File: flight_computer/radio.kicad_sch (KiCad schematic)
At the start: 3 parts, among them J4 Conn_01x07

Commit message: Schematic connecting
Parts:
- added R15 (x2): 1M, Resistor_SMD:R_0402_1005Metric, symbol Device:R
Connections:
- net GND: now also R15.1, R15.1; no longer J4.6 (Pin_6), R1.2
- net MODE_0: now also R15.2
- net MODE_1: now also R15.2
- new net VCC: J4.6 (Pin_6), R1.2
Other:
- note added: "default pull down for normal operation"
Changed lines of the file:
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@@
 (kicad_sch (version 20230121) (generator eeschema)
   (paper "A4")
-  (junction (at 153.67 101.6) (diameter 0) (color 0 0 0 0)
-  )
   (junction (at 147.32 99.06) (diameter 0) (color 0 0 0 0)
   )
+  (junction (at 140.97 88.9) (diameter 0) (color 0 0 0 0)
+  )
+  (junction (at 151.13 118.11) (diameter 0) (color 0 0 0 0)
+  )
+  (junction (at 140.97 76.2) (diameter 0) (color 0 0 0 0)
+  )
   (junction (at 124.46 96.52) (diameter 0) (color 0 0 0 0)
   )
-  (junction (at 153.67 99.06) (diameter 0) (color 0 0 0 0)
-  )
-  (wire (pts (xy 119.38 86.36) (xy 153.67 86.36))
-    (stroke (width 0) (type default))
-  )
-  (wire (pts (xy 153.67 101.6) (xy 153.67 99.06))
+  (junction (at 133.35 86.36) (diameter 0) (color 0 0 0 0)
+  )
+  (wire (pts (xy 119.38 86.36) (xy 133.35 86.36))
+    (stroke (width 0) (type default))
+  )
+  (wire (pts (xy 133.35 78.74) (xy 133.35 76.2))
+    (stroke (width 0) (type default))
+  )
+  (wire (pts (xy 176.53 118.11) (xy 151.13 118.11))
     (stroke (width 0) (type default))
   )
@@
     (stroke (width 0) (type default))
   )
-  (wire (pts (xy 151.13 118.11) (xy 151.13 101.6))
-    (stroke (width 0) (type default))
-  )
-  (wire (pts (xy 119.38 88.9) (xy 153.67 88.9))
+  (wire (pts (xy 176.53 76.2) (xy 176.53 118.11))
+    (stroke (width 0) (type default))
+  )
+  (wire (pts (xy 140.97 88.9) (xy 153.67 88.9))
+    (stroke (width 0) (type default))
+  )
+  (wire (pts (xy 151.13 101.6) (xy 151.13 118.11))
+    (stroke (width 0) (type default))
+  )
+  (wire (pts (xy 119.38 88.9) (xy 140.97 88.9))
     (stroke (width 0) (type default))
   )
@@
     (stroke (width 0) (type default))
   )
+  (wire (pts (xy 140.97 81.28) (xy 140.97 76.2))
+    (stroke (width 0) (type default))
+  )
+  (wire (pts (xy 140.97 76.2) (xy 176.53 76.2))
+    (stroke (width 0) (type default))
+  )
+  (wire (pts (xy 133.35 76.2) (xy 140.97 76.2))
+    (stroke (width 0) (type default))
+  )
   (wire (pts (xy 151.13 101.6) (xy 153.67 101.6))
     (stroke (width 0) (type default))
@@
   )
   (wire (pts (xy 119.38 96.52) (xy 124.46 96.52))
+    (stroke (width 0) (type default))
+  )
+  (wire (pts (xy 133.35 86.36) (xy 153.67 86.36))
     (stroke (width 0) (type default))
   )
@@
     (effects (font (size 1.27 1.27)) (justify left bottom))
   )
+  (text "default pull down for normal operation" (at 130.81 74.93 0)
+    (effects (font (size 1.27 1.27)) (justify left bottom))
+  )
   (text "AUX low when busy" (at 91.44 97.79 0)
     (effects (font (size 1.27 1.27)) (justify left bottom))
@@
   (hierarchical_label "TXD" (shape output) (at 119.38 93.98 180) (fields_autoplaced)
     (effects (font (size 1.27 1.27)) (justify right))
+  )
+  (symbol (lib_id "Device:R") (at 133.35 82.55 0) (unit 1)
+    (in_bom yes) (on_board yes) (dnp no) (fields_autoplaced)
+    (property "Reference" "R15" (at 135.89 81.28 0)
+      (effects (font (size 1.27 1.27)) (justify left))
+    )
+    (property "Value" "1M" (at 135.89 83.82 0)
+      (effects (font (size 1.27 1.27)) (justify left))
+    )
+    (property "Footprint" "Resistor_SMD:R_0402_1005Metric" (at 131.572 82.55 90)
+      (effects (font (size 1.27 1.27)) hide)
+    )
+    (property "Datasheet" "https://wmsc.lcsc.com/wmsc/upload/file/pdf/v2/lcsc/2206010030_UNI-ROYAL-Uniroyal-Elec-0402WGF1004TCE_C26083.pdf" (at 133.35 82.55 0)
+      (effects (font (size 1.27 1.27)) hide)
+    )
+    (property "Manufacturer PN" "0402WGF1004TCE" (at 133.35 82.55 0)
+      (effects (font (size 1.27 1.27)) hide)
+    )
+    (property "Supplier PN" "C26083" (at 133.35 82.55 0)
+      (effects (font (size 1.27 1.27)) hide)
+    )
+    (property "Supplier" "JLC" (at 133.35 82.55 0)
+      (effects (font (size 1.27 1.27)) hide)
+    )
+    (pin "1")
+    (pin "2")
+    (instances
+      (project "flight_computer"
+        (path "/89a81c02-14e9-456f-a334-ff69a24bd093/ebc948db-a9d3-410a-bdbf-1c31db890e56"
+          (reference "R15") (unit 1)
+        )
+        (path "/89a81c02-14e9-456f-a334-ff69a24bd093/0b835f18-e97c-4530-9363-7eee1af6da75"
+          (reference "R22") (unit 1)
+        )
+      )
+    )
   )
   (symbol (lib_id "Device:R") (at 138.43 99.06 90) (mirror x) (unit 1)
@@
         )
       )
+    )
+  )
+  (symbol (lib_id "Device:R") (at 140.97 85.09 0) (unit 1)
+    (in_bom yes) (on_board yes) (dnp no) (fields_autoplaced)
+    (property "Reference" "R15" (at 143.51 83.82 0)
+      (effects (font (size 1.27 1.27)) (justify left))
+    )
+    (property "Value" "1M" (at 143.51 86.36 0)
+      (effects (font (size 1.27 1.27)) (justify left))
+    )
+    (property "Footprint" "Resistor_SMD:R_0402_1005Metric" (at 139.192 85.09 90)
+      (effects (font (size 1.27 1.27)) hide)
+    )
+    (property "Datasheet" "https://wmsc.lcsc.com/wmsc/upload/file/pdf/v2/lcsc/2206010030_UNI-ROYAL-Uniroyal-Elec-0402WGF1004TCE_C26083.pdf" (at 140.97 85.09 0)
+      (effects (font (size 1.27 1.27)) hide)
+    )
+    (property "Manufacturer PN" "0402WGF1004TCE" (at 140.97 85.09 0)
+      (effects (font (size 1.27 1.27)) hide)
+    )
+    (property "Supplier PN" "C26083" (at 140.97 85.09 0)
+      (effects (font (size 1.27 1.27)) hide)
+    )
+    (property "Supplier" "JLC" (at 140.97 85.09 0)
+      (effects (font (size 1.27 1.27)) hide)
+    )
+    (pin "1")
+    (pin "2")
+    (instances
+      (project "flight_computer"
+        (path "/89a81c02-14e9-456f-a334-ff69a24bd093/ebc948db-a9d3-410a-bdbf-1c31db890e56"
+          (reference "R15") (unit 1)
+        )
+        (path "/89a81c02-14e9-456f-a334-ff69a24bd093/0b835f18-e97c-4530-9363-7eee1af6da75"
+          (reference "R23") (unit 1)
+        )
+      )

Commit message: Part way through review
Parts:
- J4: footprint (none) -> Connector_PinHeader_2.54mm:PinHeader_1x07_P2.54mm_Vertical; now left out of the parts list
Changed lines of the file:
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@@
         )
         (path "/89a81c02-14e9-456f-a334-ff69a24bd093/0b835f18-e97c-4530-9363-7eee1af6da75"
-          (reference "R22") (unit 1)
+          (reference "R21") (unit 1)
         )
       )
@@
         )
         (path "/89a81c02-14e9-456f-a334-ff69a24bd093/0b835f18-e97c-4530-9363-7eee1af6da75"
-          (reference "R18") (unit 1)
+          (reference "R22") (unit 1)
         )
       )
@@
   )
   (symbol (lib_id "Connector_Generic:Conn_01x07") (at 158.75 93.98 0) (unit 1)
-    (in_bom yes) (on_board yes) (dnp no) (fields_autoplaced)
+    (in_bom no) (on_board yes) (dnp no) (fields_autoplaced)
     (property "Reference" "J4" (at 161.29 92.71 0)
       (effects (font (size 1.27 1.27)) (justify left))
@@
       (effects (font (size 1.27 1.27)) (justify left))
     )
-    (property "Footprint" "" (at 158.75 93.98 0)
+    (property "Footprint" "Connector_PinHeader_2.54mm:PinHeader_1x07_P2.54mm_Vertical" (at 158.75 93.98 0)
       (effects (font (size 1.27 1.27)) hide)
     )
@@
       (effects (font (size 1.27 1.27)) hide)
     )
+    (property "Manufacturer PN" "~" (at 158.75 93.98 0)
+      (effects (font (size 1.27 1.27)) hide)
+    )
+    (property "Supplier PN" "~" (at 158.75 93.98 0)
+      (effects (font (size 1.27 1.27)) hide)
+    )
+    (property "Supplier" "~" (at 158.75 93.98 0)
+      (effects (font (size 1.27 1.27)) hide)
+    )

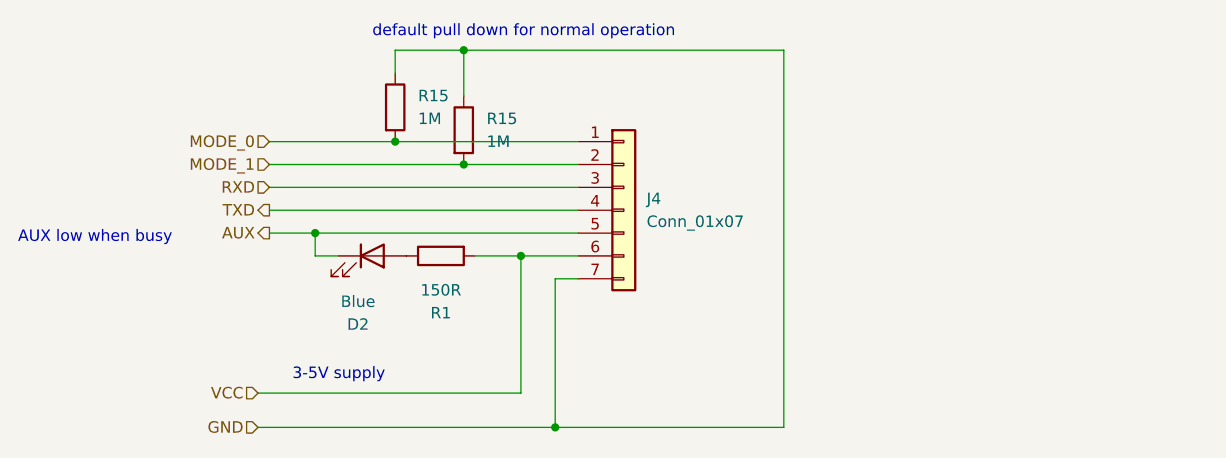
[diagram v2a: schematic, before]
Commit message: finsihed grouping the layout
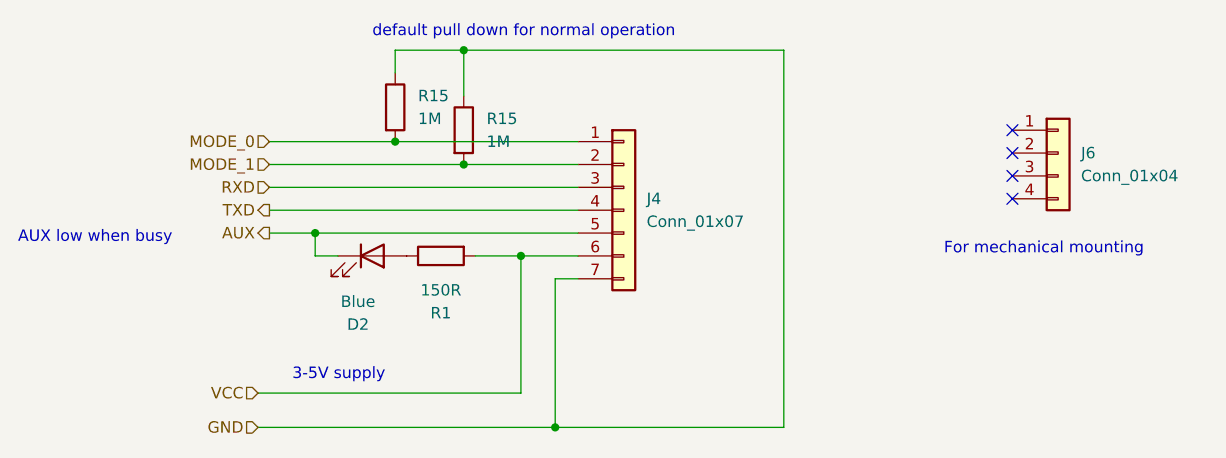
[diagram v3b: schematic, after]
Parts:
- added J6: Conn_01x04, Connector_PinHeader_2.54mm:PinHeader_1x04_P2.54mm_Vertical, symbol Connector_Generic:Conn_01x04
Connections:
- no-connect marks 0 -> 4
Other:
- note added: "For mechanical mounting"
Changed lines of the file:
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@@
   (junction (at 133.35 86.36) (diameter 0) (color 0 0 0 0)
   )
+  (no_connect (at 201.93 87.63))
+  (no_connect (at 201.93 85.09))
+  (no_connect (at 201.93 90.17))
+  (no_connect (at 201.93 92.71))
   (wire (pts (xy 119.38 86.36) (xy 133.35 86.36))
     (stroke (width 0) (type default))
@@
     (effects (font (size 1.27 1.27)) (justify left bottom))
   )
+  (text "For mechanical mounting" (at 194.31 99.06 0)
+    (effects (font (size 1.27 1.27)) (justify left bottom))
+  )
   (hierarchical_label "VCC" (shape input) (at 118.11 114.3 180) (fields_autoplaced)
     (effects (font (size 1.27 1.27)) (justify right))
@@
     (effects (font (size 1.27 1.27)) (justify right))
   )
+  (symbol (lib_id "Connector_Generic:Conn_01x04") (at 207.01 87.63 0) (unit 1)
+    (in_bom no) (on_board yes) (dnp no) (fields_autoplaced)
+    (property "Reference" "J6" (at 209.55 87.63 0)
+      (effects (font (size 1.27 1.27)) (justify left))
+    )
+    (property "Value" "Conn_01x04" (at 209.55 90.17 0)
+      (effects (font (size 1.27 1.27)) (justify left))
+    )
+    (property "Footprint" "Connector_PinHeader_2.54mm:PinHeader_1x04_P2.54mm_Vertical" (at 207.01 87.63 0)
+      (effects (font (size 1.27 1.27)) hide)
+    )
+    (property "Datasheet" "~" (at 207.01 87.63 0)
+      (effects (font (size 1.27 1.27)) hide)
+    )
+    (property "Manufacturer PN" "~" (at 207.01 87.63 0)
+      (effects (font (size 1.27 1.27)) hide)
+    )
+    (property "Supplier PN" "~" (at 207.01 87.63 0)
+      (effects (font (size 1.27 1.27)) hide)
+    )
+    (property "Supplier" "~" (at 207.01 87.63 0)
+      (effects (font (size 1.27 1.27)) hide)
+    )
+    (pin "1")
+    (pin "2")
+    (pin "3")
+    (pin "4")
+    (instances
+      (project "flight_computer"
+        (path "/89a81c02-14e9-456f-a334-ff69a24bd093/0b835f18-e97c-4530-9363-7eee1af6da75"
+          (reference "J6") (unit 1)
+        )
+      )
+    )
+  )
   (symbol (lib_id "Device:R") (at 133.35 82.55 0) (unit 1)

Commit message: Layout first effort done
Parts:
- added C1: 100nF, Capacitor_SMD:C_0402_1005Metric, symbol Device:C
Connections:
- net GND: now also C1.2
- net VCC: now also C1.1
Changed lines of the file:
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@@
 (kicad_sch (version 20230121) (generator eeschema)
   (paper "A4")
-  (junction (at 147.32 99.06) (diameter 0) (color 0 0 0 0)
-  )
   (junction (at 140.97 88.9) (diameter 0) (color 0 0 0 0)
   )
   (junction (at 151.13 118.11) (diameter 0) (color 0 0 0 0)
   )
+  (junction (at 148.59 99.06) (diameter 0) (color 0 0 0 0)
+  )
   (junction (at 140.97 76.2) (diameter 0) (color 0 0 0 0)
+  )
+  (junction (at 138.43 118.11) (diameter 0) (color 0 0 0 0)
+  )
+  (junction (at 138.43 110.49) (diameter 0) (color 0 0 0 0)
   )
   (junction (at 124.46 96.52) (diameter 0) (color 0 0 0 0)
@@
     (stroke (width 0) (type default))
   )
-  (wire (pts (xy 147.32 114.3) (xy 147.32 99.06))
+  (wire (pts (xy 138.43 118.11) (xy 151.13 118.11))
+    (stroke (width 0) (type default))
+  )
+  (wire (pts (xy 148.59 110.49) (xy 148.59 99.06))
+    (stroke (width 0) (type default))
+  )
+  (wire (pts (xy 138.43 110.49) (xy 148.59 110.49))
+    (stroke (width 0) (type default))
+  )
+  (wire (pts (xy 148.59 99.06) (xy 153.67 99.06))
     (stroke (width 0) (type default))
   )
@@
     (stroke (width 0) (type default))
   )
-  (wire (pts (xy 142.24 99.06) (xy 147.32 99.06))
-    (stroke (width 0) (type default))
-  )
   (wire (pts (xy 140.97 81.28) (xy 140.97 76.2))
     (stroke (width 0) (type default))
@@
     (stroke (width 0) (type default))
   )
-  (wire (pts (xy 118.11 118.11) (xy 151.13 118.11))
+  (wire (pts (xy 118.11 118.11) (xy 138.43 118.11))
     (stroke (width 0) (type default))
   )
@@
     (stroke (width 0) (type default))
   )
-  (wire (pts (xy 118.11 114.3) (xy 147.32 114.3))
+  (wire (pts (xy 142.24 99.06) (xy 148.59 99.06))
+    (stroke (width 0) (type default))
+  )
+  (wire (pts (xy 118.11 110.49) (xy 138.43 110.49))
     (stroke (width 0) (type default))
   )
@@
     (stroke (width 0) (type default))
   )
-  (wire (pts (xy 147.32 99.06) (xy 153.67 99.06))
-    (stroke (width 0) (type default))
-  )
-  (text "3-5V supply" (at 121.92 113.03 0)
+  (text "3-5V supply" (at 123.19 109.22 0)
     (effects (font (size 1.27 1.27)) (justify left bottom))
   )
@@
     (effects (font (size 1.27 1.27)) (justify left bottom))
   )
-  (hierarchical_label "VCC" (shape input) (at 118.11 114.3 180) (fields_autoplaced)
+  (hierarchical_label "VCC" (shape input) (at 118.11 110.49 180) (fields_autoplaced)
     (effects (font (size 1.27 1.27)) (justify right))
   )
@@
         )
       )
+    )
+  )
+  (symbol (lib_id "Device:C") (at 138.43 114.3 0) (unit 1)
+    (in_bom yes) (on_board yes) (dnp no)
+    (property "Reference" "C1" (at 142.24 113.03 0)
+      (effects (font (size 1.27 1.27)) (justify left))
+    )
+    (property "Value" "100nF" (at 142.24 115.57 0)
+      (effects (font (size 1.27 1.27)) (justify left))
+    )
+    (property "Footprint" "Capacitor_SMD:C_0402_1005Metric" (at 139.3952 118.11 0)
+      (effects (font (size 1.27 1.27)) hide)
+    )
+    (property "Datasheet" "https://wmsc.lcsc.com/wmsc/upload/file/pdf/v2/lcsc/2304140030_Samsung-Electro-Mechanics-CL05B104KO5NNNC_C1525.pdf" (at 138.43 114.3 0)
+      (effects (font (size 1.27 1.27)) hide)
+    )
+    (property "Manufacturer PN" "CL05B104KO5NNNC" (at 138.43 114.3 0)
+      (effects (font (size 1.27 1.27)) hide)
+    )
+    (property "Supplier PN" "C1525" (at 138.43 114.3 0)
+      (effects (font (size 1.27 1.27)) hide)
+    )
+    (property "Supplier" "JLC" (at 138.43 114.3 0)
+      (effects (font (size 1.27 1.27)) hide)
+    )
+    (property "Voltage" "16V" (at 133.35 114.3 0)
+      (effects (font (size 1.27 1.27)))
+    )
+    (pin "1")
+    (pin "2")
+    (instances
+      (project "flight_computer"
+        (path "/89a81c02-14e9-456f-a334-ff69a24bd093/ebc948db-a9d3-410a-bdbf-1c31db890e56"
+          (reference "C1") (unit 1)
+        )
+        (path "/89a81c02-14e9-456f-a334-ff69a24bd093/60625ff5-21c7-44a3-8ce9-cc38254a738b"
+          (reference "C4") (unit 1)
+        )
+        (path "/89a81c02-14e9-456f-a334-ff69a24bd093/0b835f18-e97c-4530-9363-7eee1af6da75"
+          (reference "C38") (unit 1)
+        )
+      )

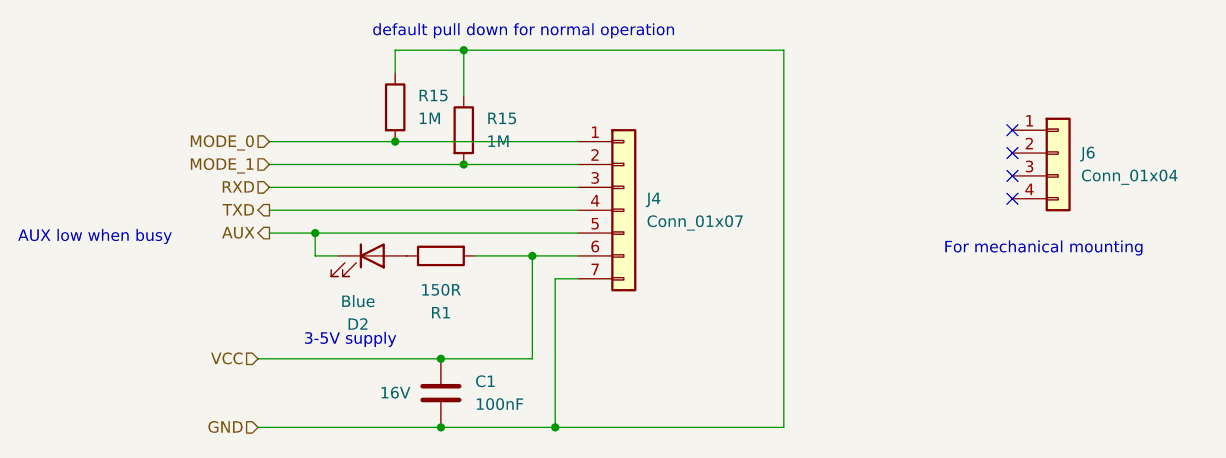
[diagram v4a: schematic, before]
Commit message: Adding E220-400T30D footprint and 3D model
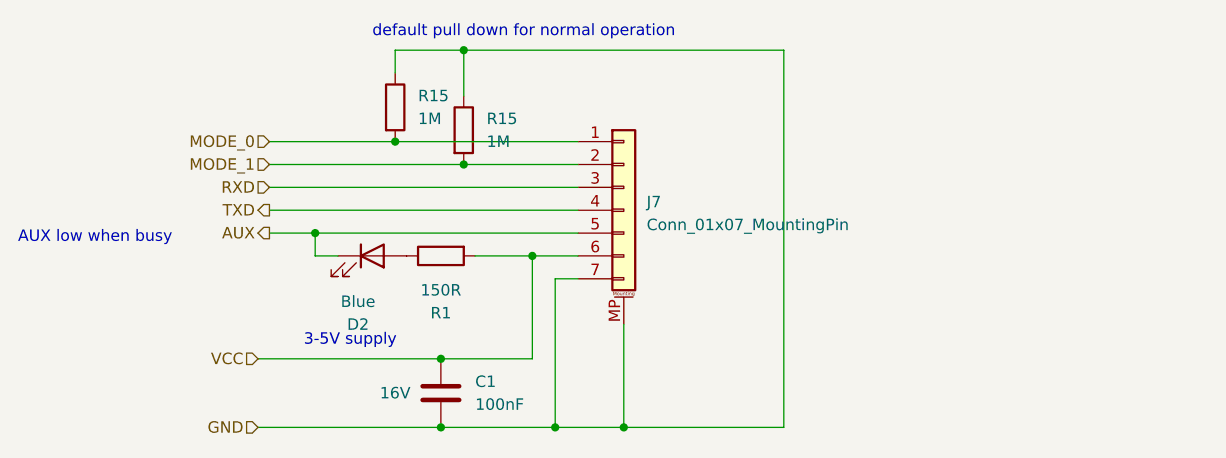
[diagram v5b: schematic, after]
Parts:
- removed J4: Conn_01x07, Connector_PinHeader_2.54mm:PinHeader_1x07_P2.54mm_Vertical, symbol Connector_Generic:Conn_01x07
- removed J6: Conn_01x04, Connector_PinHeader_2.54mm:PinHeader_1x04_P2.54mm_Vertical, symbol Connector_Generic:Conn_01x04
- added J7: Conn_01x07_MountingPin, my_footprints:E220-400T30D, symbol Connector_Generic_MountingPin:Conn_01x07_MountingPin
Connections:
- net AUX: now also J7.5 (Pin_5)
- net GND: now also J7.7 (Pin_7), J7.MP (MountPin)
- net MODE_0: now also J7.1 (Pin_1)
- net MODE_1: now also J7.2 (Pin_2)
- net RXD: now also J7.3 (Pin_3)
- net TXD: now also J7.4 (Pin_4)
- net VCC: now also J7.6 (Pin_6)
- no-connect marks 4 -> 0
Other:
- note removed: "For mechanical mounting"
